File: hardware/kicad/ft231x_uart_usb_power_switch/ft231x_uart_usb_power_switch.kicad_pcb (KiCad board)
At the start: 2 copper layers, 50.8 x 22.8 mm, 57 parts, among them J1 USB_B_Micro_ALT, J2 USB_A_ALT, J3 Conn_01x04, SW1 PTS810SJK250SMTRLFS, U1 SRV05-4, U2 FT231XS, U3 TPS2553DBVR, U4 SN74LVC3G04DCTR, U5 NC7SZ66M5X

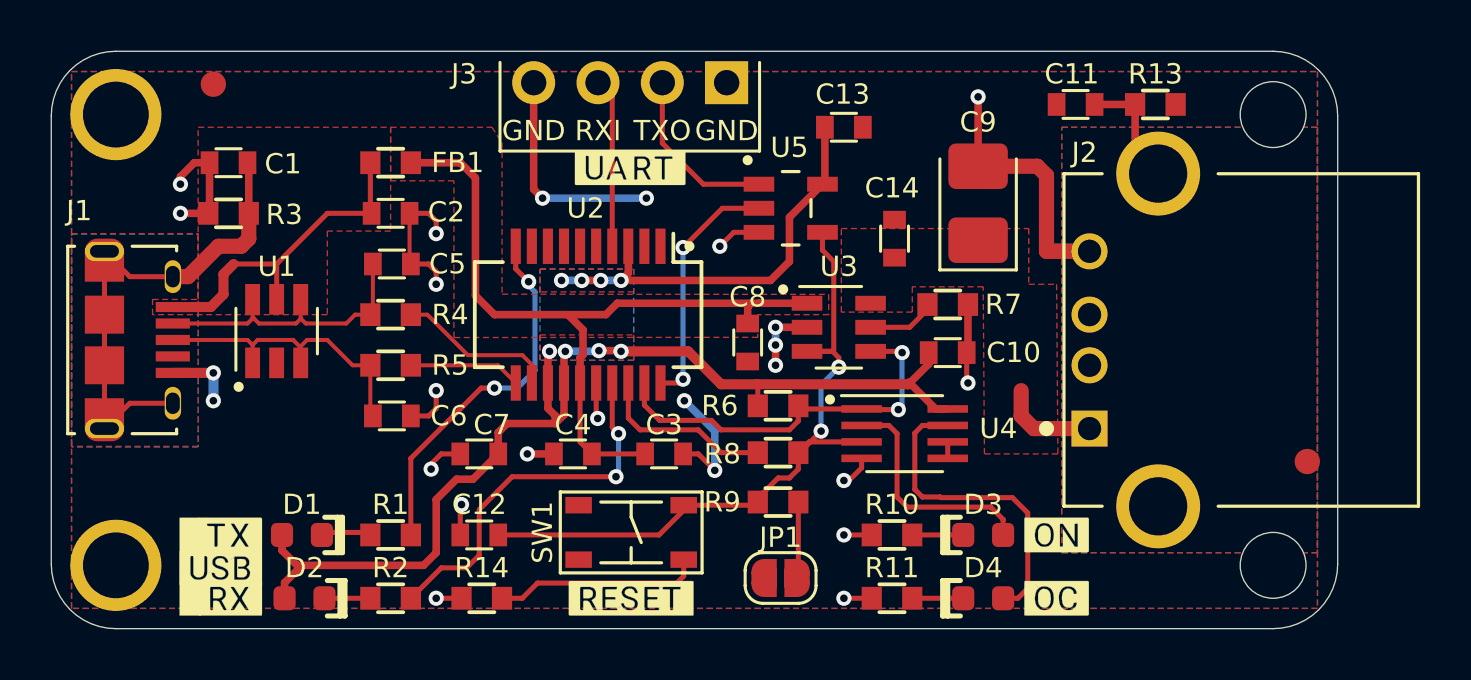
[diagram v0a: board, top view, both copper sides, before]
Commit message: Update Design Based On Feedback
* Add Power LED
* Add 3.3V to header
* Swap RX and TX Label (This was labelled from USB perspective, now labelled from UART perspective)
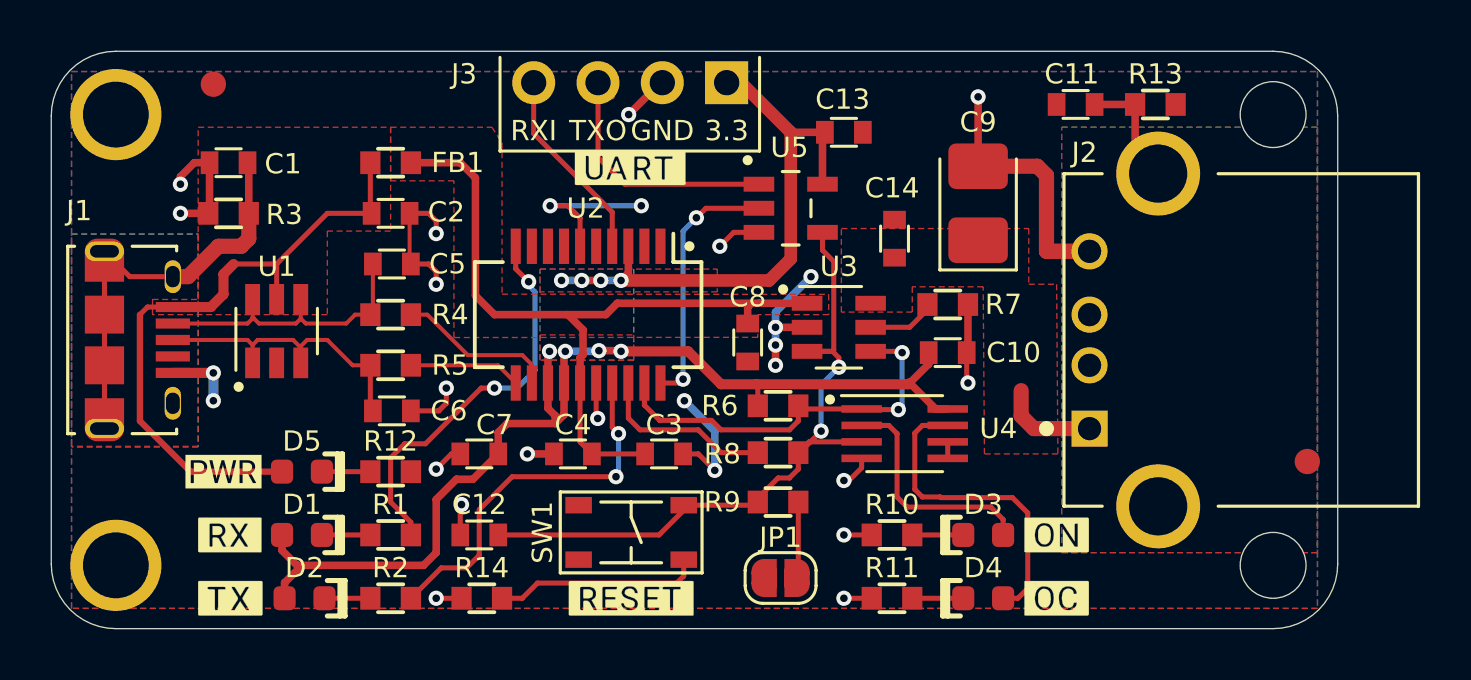
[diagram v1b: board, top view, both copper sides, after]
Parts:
- removed the ? at (121.3, 129.0)
- added D5: LED, -Discrete:LED_0603_1608Metric, F.Cu at (124.5, 125.2)
- added R12: 10k, -Passive:R_0603, F.Cu at (128.0, 125.2)
- added kibuzzard-61683F86: G***, label, F.Cu at (121.4, 125.2)
- moved ? 2.50 mm to (121.7, 130.2)
- moved ? 2.50 mm to (121.7, 127.7)
- moved C13 0.20 mm to (145.9, 111.8)
- moved C6 0.20 mm to (128.1, 122.8)
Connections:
- net Net-(C2-Pad1) renamed VBUS
- J3 pad 1: GND -> +3V3
- J3 pad 2: /STXD -> GND
- J3 pad 3: /RXD -> /STXD
- J3 pad 4: GND -> /RXD
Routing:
- net VBUS: track 13.3 -> 25.3 mm
- net +3V3: track 58.7 -> 64.9 mm
- net /STXD: track 6.88 -> 10.5 mm
- net Net-(C1-Pad1): track 19.9 -> 16.8 mm
- net Net-(D5-Pad1): track 0.00 -> 1.91 mm
- net GND: track 57.6 -> 59.3 mm, vias 25 -> 27
- net /TXLED: track 14.6 -> 15.7 mm
- net /RXD: track 6.69 -> 7.75 mm

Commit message: Update source files to kicad 6
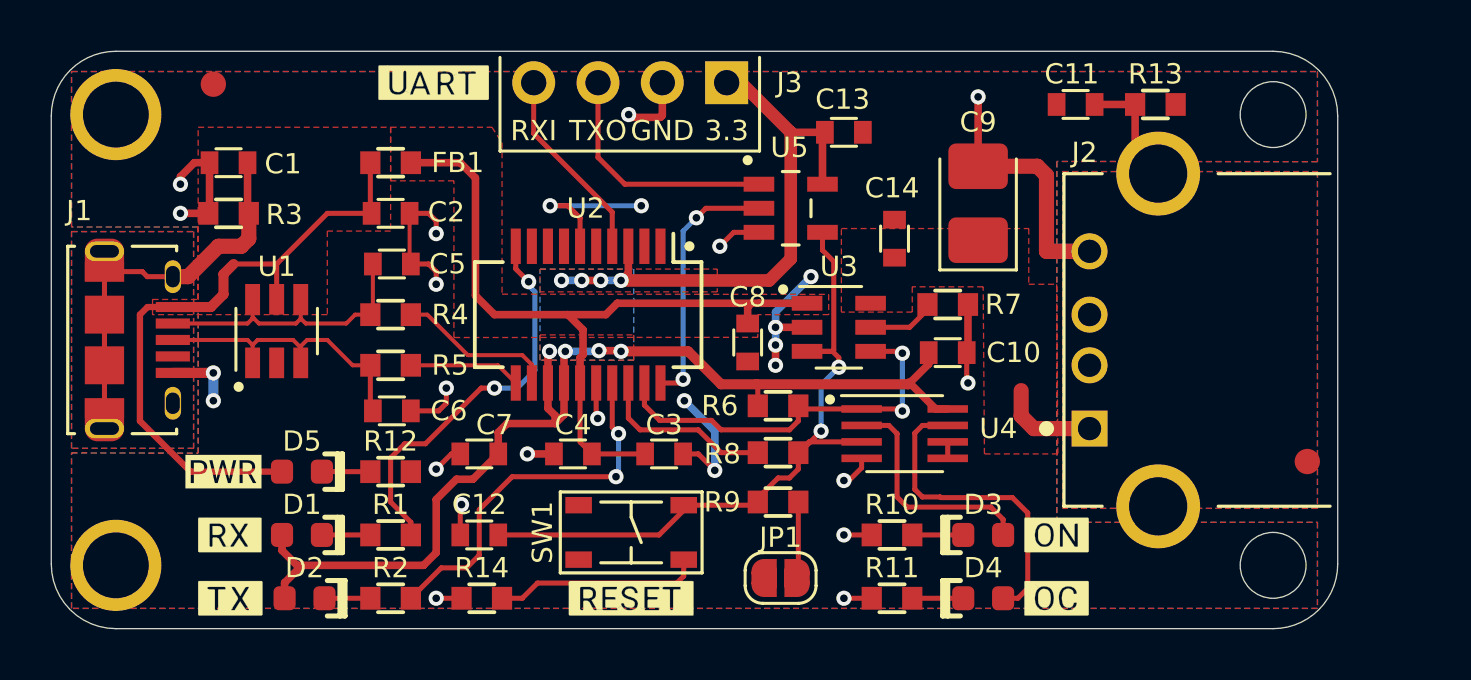
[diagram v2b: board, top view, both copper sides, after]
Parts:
- R12: value 10k -> 2k
- moved ? 8.46 mm to (129.7, 109.8)
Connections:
- net /FAULT renamed /GPI
- net /~EN renamed /~{EN}
- J1 pad 4: Net-(J1-Pad4) -> unconnected-(J1-Pad4)
- J2 pad 2: Net-(J2-Pad2) -> unconnected-(J2-Pad2)
- J2 pad 3: Net-(J2-Pad3) -> unconnected-(J2-Pad3)
- SW1 pad 2: Net-(SW1-Pad2) -> unconnected-(SW1-Pad2)
- SW1 pad 4: Net-(SW1-Pad4) -> unconnected-(SW1-Pad4)
- U2 pad 1: Net-(U2-Pad1) -> unconnected-(U2-Pad1)
- U2 pad 2: Net-(U2-Pad2) -> unconnected-(U2-Pad2)
- U2 pad 5: Net-(U2-Pad5) -> unconnected-(U2-Pad5)
- U2 pad 7: Net-(U2-Pad7) -> unconnected-(U2-Pad7)
- U2 pad 8: Net-(U2-Pad8) -> unconnected-(U2-Pad8)
- U2 pad 9: Net-(U2-Pad9) -> unconnected-(U2-Pad9)
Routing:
- net Net-(C1-Pad1): track 16.8 -> 14.8 mm
- net Net-(C14-Pad1): track 5.66 -> 3.91 mm
- net Net-(D3-Pad2): track 10.1 -> 9.20 mm
- net GND: track 59.3 -> 60.1 mm
- net /STXD: track 10.5 -> 9.74 mm
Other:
- net class Default removed

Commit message: Update revision to 0.4
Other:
- board text added: "v0.4<<hash>>"
- board text removed: "v0.3<<hash>>"
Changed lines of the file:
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@@
   (title_block
     (title "ft231x uart usb power switch")
-    (date "2021-03-25")
-    (rev "0.30")
+    (date "2022-02-07")
+    (rev "0.40")
   )
   (layers
@@
   (gr_line (start 162.85 108.6) (end 117.15 108.6) (layer "Edge.Cuts") (width 0.05))
   (gr_arc (start 114.600001 111.15) (mid 115.346878 109.346878) (end 117.15 108.600001) (layer "Edge.Cuts") (width 0.05))
-  (gr_text "v0.3<<hash>>" (at 152.4 121) (layer "B.SilkS")
+  (gr_text "v0.4<<hash>>" (at 152.4 121) (layer "B.SilkS")
     (effects (font (size 1 1) (thickness 0.15)) (justify left mirror))
   )

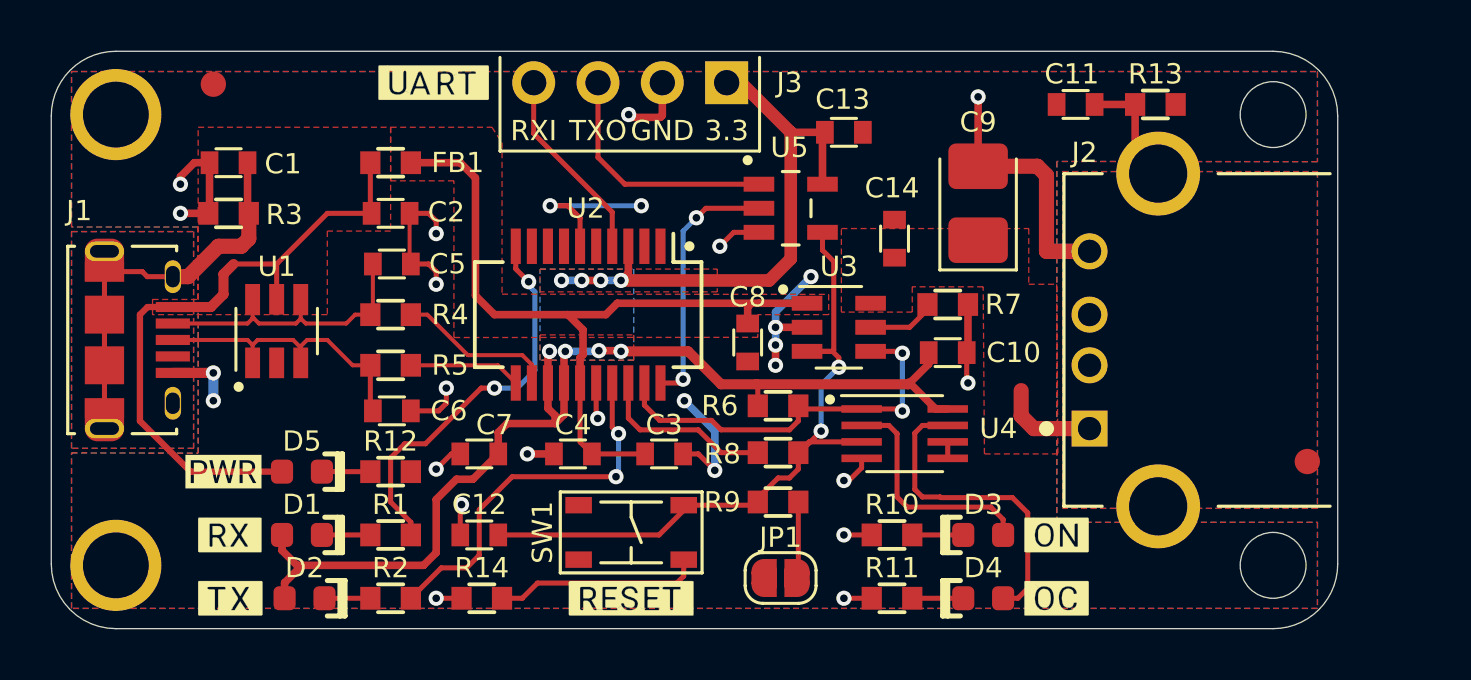
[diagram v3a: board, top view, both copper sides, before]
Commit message: Increase size of kibuzzard labels
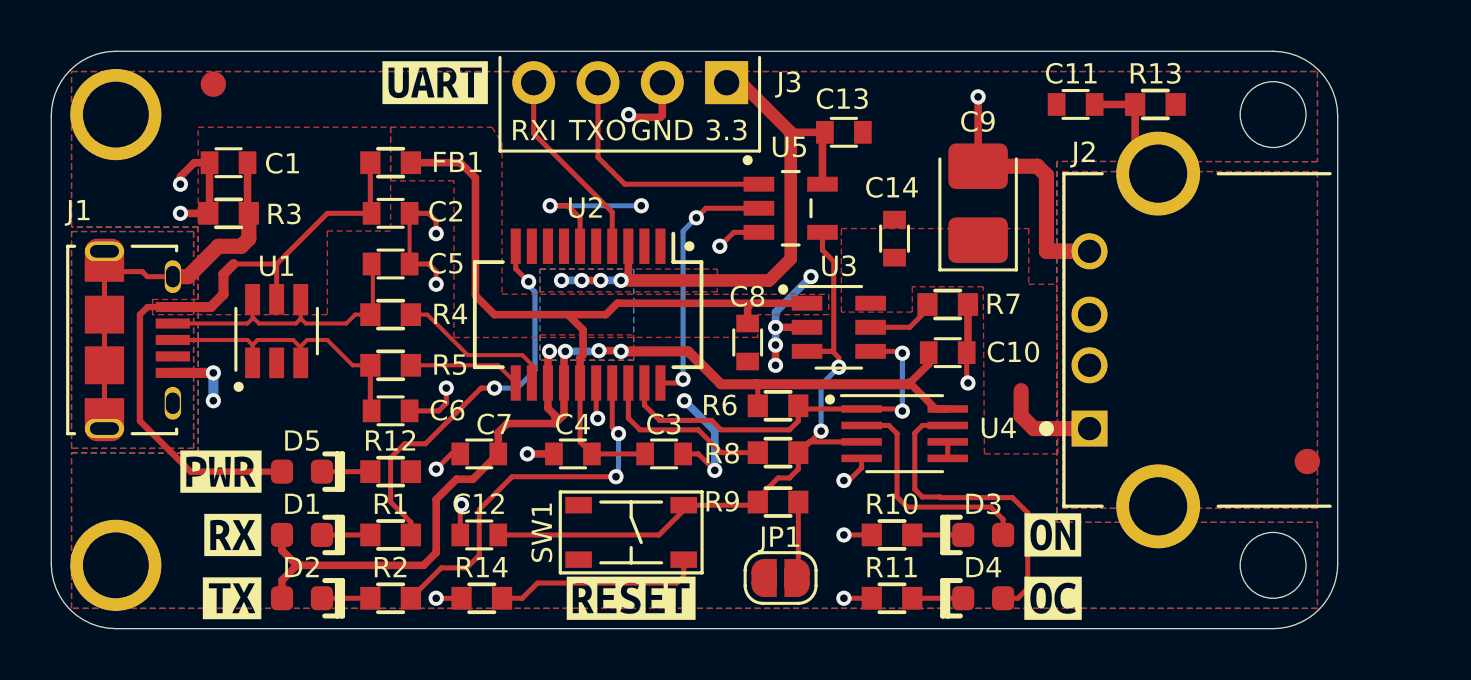
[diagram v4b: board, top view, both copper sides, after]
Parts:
- removed ? (x6): , buzzard_labels
- removed kibuzzard-61683F86: G***, label
- added kibuzzard-6210B9B1: G***, kibuzzard-6210B9B1, F.Cu at (137.5, 130.2)
- added kibuzzard-6210BA32: G***, kibuzzard-6210BA32, F.Cu at (121.3, 125.2)
- added kibuzzard-6210BA40: G***, kibuzzard-6210BA40, F.Cu at (121.8, 127.7)
- added kibuzzard-6210BA4A: G***, kibuzzard-6210BA4A, F.Cu at (121.7, 130.2)
- added kibuzzard-6210BA51: G***, kibuzzard-6210BA51, F.Cu at (154.2, 130.2)
- added kibuzzard-6210BA58: G***, kibuzzard-6210BA58, F.Cu at (154.2, 127.7)
- added kibuzzard-6210BA5D: G***, kibuzzard-6210BA5D, F.Cu at (129.8, 109.8)
- moved D2 0.10 mm to (124.5, 130.2)
- moved C5 0.05 mm to (128.0, 117.0)
- moved C6 0.05 mm to (128.0, 122.8)
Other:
- board text added: "v0.5<<hash>>"
- board text removed: "v0.4<<hash>>"

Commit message: Open up solder paste holes for mechanical pins Micro USB
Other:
- rule pad_to_mask_clearance: 0.1 -> 0.05
- rule solder_mask_min_width: 0.25 -> 0.2
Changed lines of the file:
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@@
   )
   (setup
-    (pad_to_mask_clearance 0.1)
-    (solder_mask_min_width 0.25)
+    (stackup
+      (layer "F.SilkS" (type "Top Silk Screen"))
+      (layer "F.Paste" (type "Top Solder Paste"))
+      (layer "F.Mask" (type "Top Solder Mask") (thickness 0.01))
+      (layer "F.Cu" (type "copper") (thickness 0.035))
+      (layer "dielectric 1" (type "core") (thickness 1.51) (material "FR4") (epsilon_r 4.5) (loss_tangent 0.02))
+      (layer "B.Cu" (type "copper") (thickness 0.035))
+      (layer "B.Mask" (type "Bottom Solder Mask") (thickness 0.01))
+      (layer "B.Paste" (type "Bottom Solder Paste"))
+      (layer "B.SilkS" (type "Bottom Silk Screen"))
+      (copper_finish "None")
+      (dielectric_constraints no)
+    )
+    (pad_to_mask_clearance 0.05)
+    (solder_mask_min_width 0.2)
     (pcbplotparams
       (layerselection 0x00010fc_ffffffff)
@@
       (effects (font (size 0.393701 0.393701) (thickness 0.015)))
     )
+    (fp_line (start -3.5 -0.77) (end -3.5 -0.6) (layer "F.Paste") (width 0.0001))
     (fp_line (start 3.5 0.77) (end 3.5 0.6) (layer "F.Paste") (width 0.0001))
-    (fp_line (start -3.5 -0.77) (end -3.5 -0.6) (layer "F.Paste") (width 0.0001))
-    (fp_line (start 3.7 1.18) (end 3.7 1.45) (layer "F.SilkS") (width 0.127))
     (fp_line (start 3.7 -2.85) (end 3.7 -1.095) (layer "F.SilkS") (width 0.127))
-    (fp_line (start -3.7 -2.85) (end -3.52 -2.85) (layer "F.SilkS") (width 0.127))
-    (fp_line (start -3.7 1.45) (end 3.7 1.45) (layer "F.SilkS") (width 0.127))
+    (fp_line (start -3.7 -2.85) (end -3.7 -1.095) (layer "F.SilkS") (width 0.127))
     (fp_line (start 3.7 -2.85) (end 3.52 -2.85) (layer "F.SilkS") (width 0.127))
     (fp_line (start -3.7 1.45) (end -3.7 1.18) (layer "F.SilkS") (width 0.127))
-    (fp_line (start -3.7 -2.85) (end -3.7 -1.095) (layer "F.SilkS") (width 0.127))
+    (fp_line (start -3.7 -2.85) (end -3.52 -2.85) (layer "F.SilkS") (width 0.127))
+    (fp_line (start 3.7 1.18) (end 3.7 1.45) (layer "F.SilkS") (width 0.127))
+    (fp_line (start -3.7 1.45) (end 3.7 1.45) (layer "F.SilkS") (width 0.127))
     (fp_poly (pts
         (xy 3.6 0.875)
@@
         (xy -3.6 -0.875)
       ) (layer "F.Mask") (width 0.0001) (fill solid))
+    (fp_line (start -4.25 2.15) (end -4.25 -3.625) (layer "F.CrtYd") (width 0.05))
     (fp_line (start 4.25 2.15) (end 4.25 -3.625) (layer "F.CrtYd") (width 0.05))
+    (fp_line (start 4.725 2.93) (end -4.725 2.93) (layer "F.CrtYd") (width 0.05))
+    (fp_line (start 4.725 2.93) (end 4.25 2.15) (layer "F.CrtYd") (width 0.05))
+    (fp_line (start -4.25 -3.625) (end 4.25 -3.625) (layer "F.CrtYd") (width 0.05))
     (fp_line (start -4.725 2.93) (end -4.25 2.15) (layer "F.CrtYd") (width 0.05))
-    (fp_line (start 4.725 2.93) (end 4.25 2.15) (layer "F.CrtYd") (width 0.05))
-    (fp_line (start -4.25 2.15) (end -4.25 -3.625) (layer "F.CrtYd") (width 0.05))
-    (fp_line (start -4.25 -3.625) (end 4.25 -3.625) (layer "F.CrtYd") (width 0.05))
-    (fp_line (start 4.725 2.93) (end -4.725 2.93) (layer "F.CrtYd") (width 0.05))
+    (fp_line (start -3.7 -2.85) (end 3.7 -2.85) (layer "F.Fab") (width 0.127))
+    (fp_line (start -3.7 1.45) (end 3.7 1.45) (layer "F.Fab") (width 0.127))
     (fp_line (start -3.7 -2.85) (end -3.7 1.45) (layer "F.Fab") (width 0.127))
+    (fp_line (start 3.7 2.15) (end 3.7 1.45) (layer "F.Fab") (width 0.127))
+    (fp_line (start -4.025 2.68) (end 4.025 2.68) (layer "F.Fab") (width 0.127))
+    (fp_line (start -3.7 2.15) (end -4.025 2.68) (layer "F.Fab") (width 0.127))
     (fp_line (start -3.7 1.45) (end -3.7 2.15) (layer "F.Fab") (width 0.127))
-    (fp_line (start -3.7 2.15) (end -4.025 2.68) (layer "F.Fab") (width 0.127))
-    (fp_line (start -3.7 1.45) (end 3.7 1.45) (layer "F.Fab") (width 0.127))
-    (fp_line (start -3.7 -2.85) (end 3.7 -2.85) (layer "F.Fab") (width 0.127))
-    (fp_line (start 3.7 2.15) (end 3.7 1.45) (layer "F.Fab") (width 0.127))
+    (fp_line (start 4.025 2.68) (end 3.7 2.15) (layer "F.Fab") (width 0.127))
     (fp_line (start 3.7 1.45) (end 3.7 -2.85) (layer "F.Fab") (width 0.127))
-    (fp_line (start 4.025 2.68) (end 3.7 2.15) (layer "F.Fab") (width 0.127))
-    (fp_line (start -4.025 2.68) (end 4.025 2.68) (layer "F.Fab") (width 0.127))
     (pad "1" smd rect (at -1.3 -2.7 270) (size 0.4 1.35) (layers "F.Cu" "F.Paste" "F.Mask")
       (net 39 "VBUS") (pinfunction "VBUS") (pintype "power_out"))
@@
     (pad "5" smd rect (at 1.3 -2.7 270) (size 0.4 1.35) (layers "F.Cu" "F.Paste" "F.Mask")
       (net 2 "GND") (pinfunction "GND") (pintype "power_out"))
-    (pad "6" thru_hole oval (at -3.5 0 270) (size 0.775 1.55) (drill oval 0.5 1.15) (layers *.Cu *.Mask)
+    (pad "6" smd rect (at -1 0 270) (size 1.5 1.55) (layers "F.Cu" "F.Paste" "F.Mask")
+      (net 1 "Net-(C1-Pad1)") (pinfunction "SHIELD") (pintype "passive"))
+    (pad "6" thru_hole oval (at 3.5 0 270) (size 0.775 1.55) (drill oval 0.5 1.15) (layers *.Cu *.Mask "F.Paste")
+      (net 1 "Net-(C1-Pad1)") (pinfunction "SHIELD") (pintype "passive"))
+    (pad "6" smd rect (at 1 0 270) (size 1.5 1.55) (layers "F.Cu" "F.Paste" "F.Mask")
+      (net 1 "Net-(C1-Pad1)") (pinfunction "SHIELD") (pintype "passive"))
+    (pad "6" thru_hole oval (at -3.5 0 270) (size 0.775 1.55) (drill oval 0.5 1.15) (layers *.Cu *.Mask "F.Paste")
+      (net 1 "Net-(C1-Pad1)") (pinfunction "SHIELD") (pintype "passive"))
+    (pad "6" thru_hole oval (at -2.5 -2.7 270) (size 1.3 0.65) (drill oval 0.85 0.55) (layers *.Cu *.Mask "F.Paste")
       (net 1 "Net-(C1-Pad1)") (pinfunction "SHIELD") (pintype "passive"))
     (pad "6" smd custom (at 2.7 0 270) (size 0.775 1.55) (layers "F.Cu" "F.Paste" "F.Mask")
@@
           ) (width 0.001) (fill yes))
       ))
-    (pad "6" thru_hole oval (at 3.5 0 270) (size 0.775 1.55) (drill oval 0.5 1.15) (layers *.Cu *.Mask)
-      (net 1 "Net-(C1-Pad1)") (pinfunction "SHIELD") (pintype "passive"))
-    (pad "6" thru_hole oval (at 2.5 -2.7 270) (size 1.3 0.65) (drill oval 0.85 0.55) (layers *.Cu *.Mask)
-      (net 1 "Net-(C1-Pad1)") (pinfunction "SHIELD") (pintype "passive"))
-    (pad "6" smd rect (at 1 0 270) (size 1.5 1.55) (layers "F.Cu" "F.Paste" "F.Mask")
-      (net 1 "Net-(C1-Pad1)") (pinfunction "SHIELD") (pintype "passive"))
-    (pad "6" thru_hole oval (at -2.5 -2.7 270) (size 1.3 0.65) (drill oval 0.85 0.55) (layers *.Cu *.Mask)
-      (net 1 "Net-(C1-Pad1)") (pinfunction "SHIELD") (pintype "passive"))
     (pad "6" smd custom (at -2.7 0 270) (size 0.775 1.55) (layers "F.Cu" "F.Paste" "F.Mask")
       (net 1 "Net-(C1-Pad1)") (pinfunction "SHIELD") (pintype "passive")
@@
           ) (width 0.001) (fill yes))
       ))
-    (pad "6" smd rect (at -1 0 270) (size 1.5 1.55) (layers "F.Cu" "F.Paste" "F.Mask")
+    (pad "6" thru_hole oval (at 2.5 -2.7 270) (size 1.3 0.65) (drill oval 0.85 0.55) (layers *.Cu *.Mask "F.Paste")
       (net 1 "Net-(C1-Pad1)") (pinfunction "SHIELD") (pintype "passive"))
     (model "${KIPRJMOD}/../library/3d_model/Connector/AMPHENOL_10118194-0001LF.step"
